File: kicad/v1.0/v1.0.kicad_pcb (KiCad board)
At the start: 2 copper layers, 71.4 x 69.6 mm, 50 parts, among them J1 USB_B_Micro, J2 9V_IN, J3 MOTOR, J4 LED, J5 BUTTON, Q1 IRF520, SW1 RESET, SW2 FLASH, U1 MCP2221AxSL, U2 MAX14872ETC+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

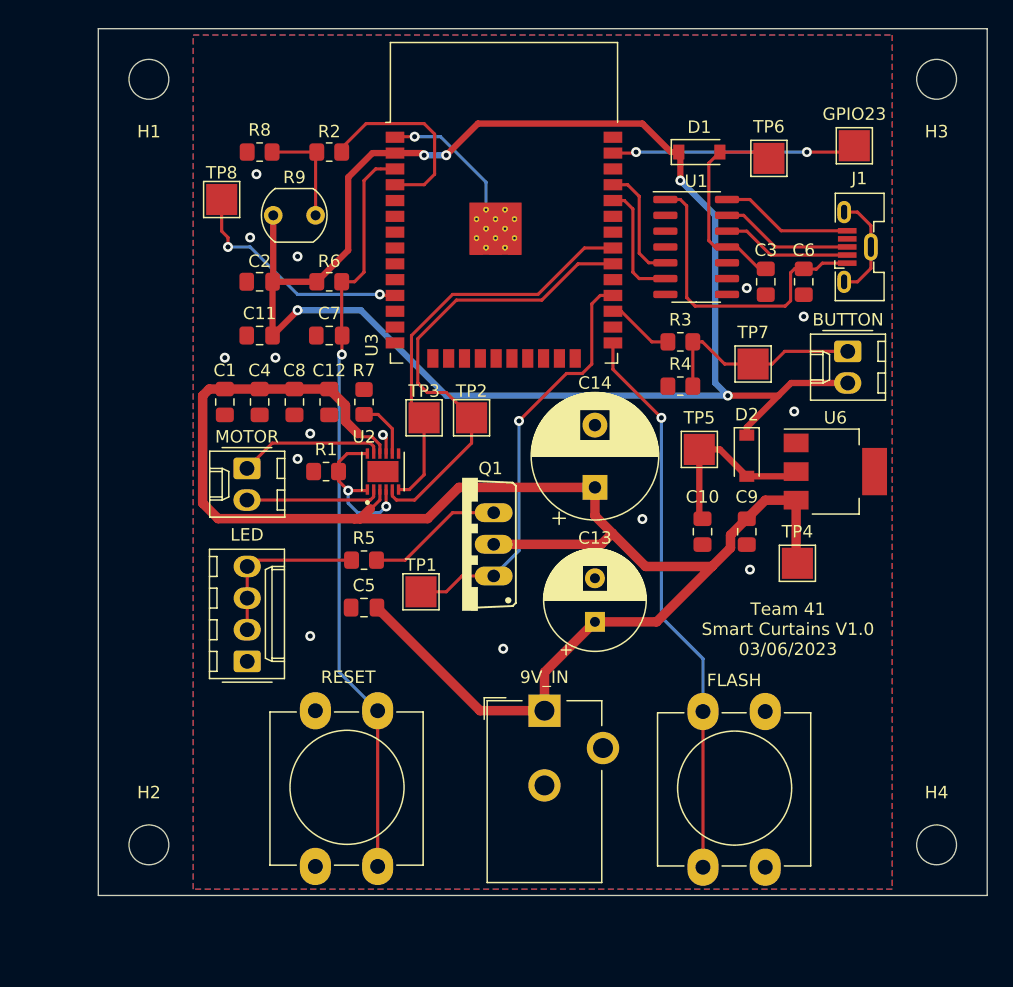
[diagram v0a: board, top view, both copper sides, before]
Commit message: v0.0 has been sent to TA for printing, all future changes must be on v1.0
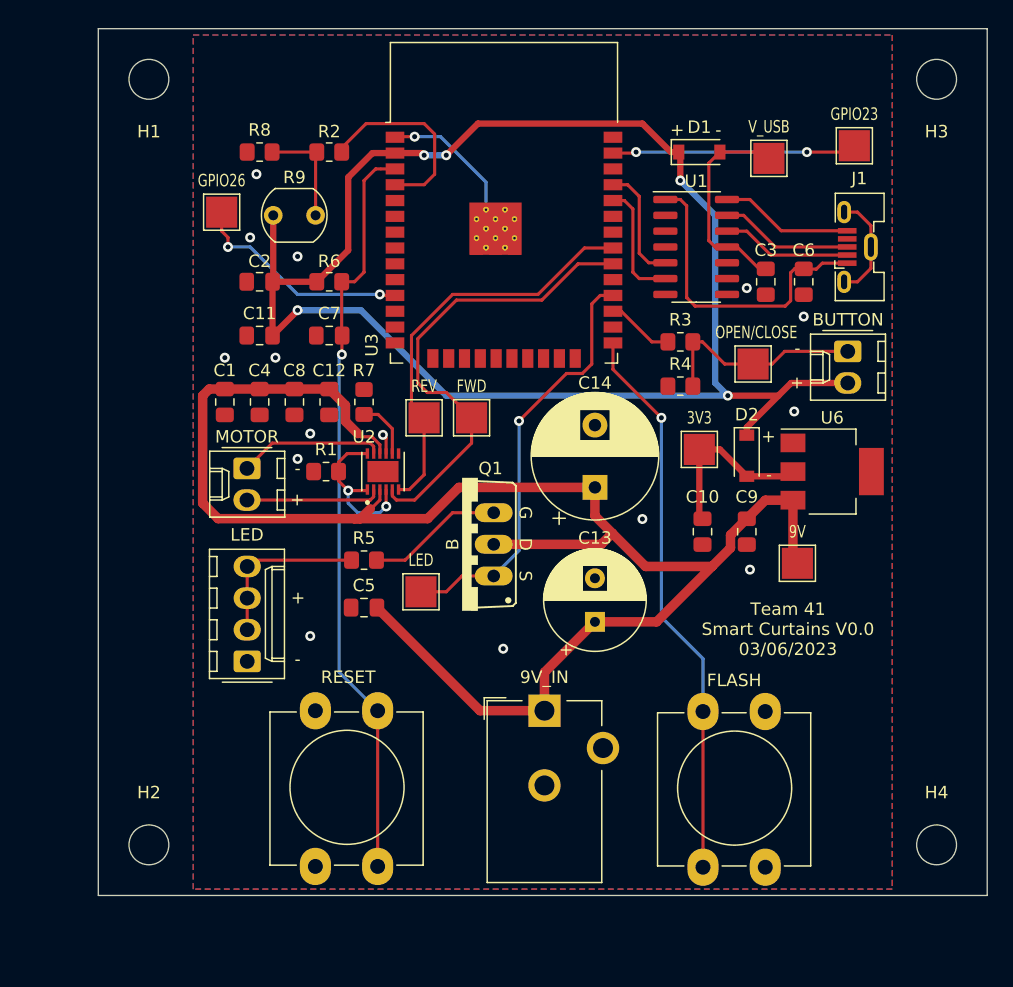
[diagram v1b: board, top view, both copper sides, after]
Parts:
- removed GPIO23: TestPoint, TestPoint:TestPoint_Pad_2.5x2.5mm
- added TP9: TestPoint, TestPoint:TestPoint_Pad_2.5x2.5mm, F.Cu at (173.5, 59.9)
- moved TP8 1.02 mm to (122.7, 65.3)
- moved U6 0.25 mm to (171.7, 86.1)
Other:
- board text added: "3V3"
- board text added: "9V"
- board text added: "FWD"
- board text added: "GPIO23"
- board text added: "GPIO26"
- board text added: "LED"
- board text added: "OPEN/CLOSE"
- board text added: "REV"
- board text added: "Team 41 Smart Curtains V0.0 03/06/2023"
- board text added: "V_USB"
- board text removed: "Team 41 Smart Curtains V1.0 03/06/2023"

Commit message: v0.0 pcb checkin
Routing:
- net Net-(J4-Pad2): track 13.7 -> 14.4 mm
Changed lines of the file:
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@@
       (effects (font (size 1 1) (thickness 0.15)))
     )
-    (fp_text user "S" (at -2.54 5.08 270 unlocked) (layer "F.SilkS")
-      (effects (font (size 1 1) (thickness 0.15)))
-    )
-    (fp_text user "G" (at 2.54 5.08 270 unlocked) (layer "F.SilkS")
+    (fp_text user "S" (at 2.54 5.08 270 unlocked) (layer "F.SilkS")
+      (effects (font (size 1 1) (thickness 0.15)))
+    )
+    (fp_text user "G" (at -2.794 5.08 270 unlocked) (layer "F.SilkS")
       (effects (font (size 1 1) (thickness 0.15)))
     )
@@
   (segment (start 133.604 89.408) (end 132.842 88.646) (width 0.254) (layer "B.Cu") (net 16))
   (segment (start 135.895714 88.905714) (end 135.884286 88.905714) (width 0.254) (layer "B.Cu") (net 16))
-  (segment (start 135.112 93.218) (end 137.414 93.218) (width 0.254) (layer "F.Cu") (net 17))
-  (segment (start 137.414 93.218) (end 141.224 89.408) (width 0.254) (layer "F.Cu") (net 17))
-  (segment (start 141.224 89.408) (end 144.526 89.408) (width 0.254) (layer "F.Cu") (net 17))
+  (segment (start 137.922 93.218) (end 135.112 93.218) (width 0.762) (layer "F.Cu") (net 17))
+  (segment (start 141.732 89.408) (end 137.922 93.218) (width 0.762) (layer "F.Cu") (net 17))
+  (segment (start 144.526 89.408) (end 141.732 89.408) (width 0.762) (layer "F.Cu") (net 17))
   (segment (start 126.73 60.452) (end 130.318 60.452) (width 0.25) (layer "F.Cu") (net 18))
   (segment (start 130.224 60.546) (end 130.318 60.452) (width 0.25) (layer "F.Cu") (net 18))
@@
   (segment (start 157.226 75.692) (end 158.512 75.692) (width 0.254) (layer "F.Cu") (net 56))
   (segment (start 124.734 93.706) (end 125.222 93.218) (width 0.254) (layer "F.Cu") (net 57))
-  (segment (start 124.734 98.806) (end 124.734 96.266) (width 0.254) (layer "F.Cu") (net 57))
   (segment (start 124.734 93.726) (end 124.734 93.706) (width 0.254) (layer "F.Cu") (net 57))
-  (segment (start 124.734 96.266) (end 124.734 93.726) (width 0.254) (layer "F.Cu") (net 57))
-  (segment (start 125.222 93.218) (end 133.112 93.218) (width 0.254) (layer "F.Cu") (net 57))
+  (segment (start 124.734 98.806) (end 124.734 96.266) (width 0.762) (layer "F.Cu") (net 57))
+  (segment (start 132.604 93.726) (end 124.734 93.726) (width 0.762) (layer "F.Cu") (net 57))
+  (segment (start 124.734 96.266) (end 124.734 93.726) (width 0.762) (layer "F.Cu") (net 57))
+  (segment (start 133.112 93.218) (end 132.604 93.726) (width 0.762) (layer "F.Cu") (net 57))
   (segment (start 163.068 77.47) (end 165.354 77.47) (width 0.254) (layer "F.Cu") (net 58))
   (segment (start 166.878 77.47) (end 167.894 76.454) (width 0.254) (layer "F.Cu") (net 58))

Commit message: getting ready to start designing PCB 1.0
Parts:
- removed R7: 10k, Resistor_SMD:R_0805_2012Metric_Pad1.20x1.40mm_HandSolder
- added C15: 22u, Capacitor_SMD:C_0805_2012Metric_Pad1.18x1.45mm_HandSolder, F.Cu at (134.6, 89.4)
- added R10: 1k, Resistor_SMD:R_0805_2012Metric_Pad1.20x1.40mm_HandSolder, F.Cu at (159.0, 102.1)
- U2: value MAX14872ETC+ -> ZXBM5210-SP; footprint MAX14872ETC_:SON50P300X300X80-13N -> Package_SO:Diodes_SO-8EP
- moved C5 11.5 mm to (145.0, 100.6)
- moved SW1 8.25 mm to (122.0, 117.8)
- moved U2 7.82 mm to (128.0, 87.9), turned to 180 degrees
- moved H1 6.37 mm to (110.5, 54.1)
- moved H2 6.37 mm to (110.5, 116.6)
- moved J3 5.87 mm to (118.9, 86.1)
- moved J4 5.85 mm to (118.9, 101.1)
- moved C1 5.84 mm to (117.1, 80.5)
- moved R1 5.61 mm to (130.6, 80.5), turned to -90 degrees
- moved C4 5.33 mm to (120.4, 80.5)
- moved C8 4.57 mm to (124.0, 80.5)
- moved C12 3.81 mm to (127.5, 80.5)
- moved J2 3.57 mm to (145.0, 105.6)
- moved SW2 2.07 mm to (163.4, 117.9)
- moved TP2 1.55 mm to (144.3, 81.5)
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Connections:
- J3 pad 1: Net-(J3-Pad1) -> Net-(U2-Pad7)
- J3 pad 2: Net-(J3-Pad2) -> Net-(U2-Pad1)
- R1 pad 1: /SNS -> +9V
- SW2 pad 1: Net-(SW2-Pad1) -> Net-(R10-Pad2)
- U2 pad 1: /SNS -> Net-(U2-Pad1)
- U2 pad 2: Net-(J3-Pad2) -> Net-(U2-Pad2)
- U2 pad 4: /SNS -> /FWD
- U2 pad 5: /FWD -> /REV
- U2 pad 6: /REV -> +9V
- U2 pad 7: unconnected-(U2-Pad7) -> Net-(U2-Pad7)
- U2 pad 8: Net-(R7-Pad1) -> GND
- U3 pad 25: Net-(SW2-Pad1) -> Net-(R10-Pad1)
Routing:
- net Net-(SW2-Pad1): track 45.1 -> 0.00 mm, vias 1 -> 0
- net Net-(R10-Pad1): track 0.00 -> 28.0 mm, vias 0 -> 2
- net Net-(R10-Pad2): track 0.00 -> 17.3 mm
- net +9V: track 137.7 -> 121.3 mm
- net Net-(U2-Pad1): track 0.00 -> 13.4 mm
- net /SNS: track 12.7 -> 0.00 mm, vias 2 -> 0
- net Net-(J3-Pad1): track 11.7 -> 0.00 mm
- net /REV: track 33.2 -> 44.9 mm, vias 0 -> 2
- net Net-(J3-Pad2): track 10.9 -> 0.00 mm
- net Net-(U2-Pad7): track 0.00 -> 7.67 mm
- net /FWD: track 38.1 -> 43.5 mm, vias 0 -> 2
- net Net-(J4-Pad2): track 14.4 -> 19.4 mm
- net Net-(R7-Pad1): track 4.75 -> 0.00 mm
- net Net-(U2-Pad2): track 0.00 -> 3.44 mm
- net Net-(C7-Pad1): track 60.7 -> 62.4 mm
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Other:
- board size 71.4 x 69.6 mm -> 77.2 x 69.6 mm

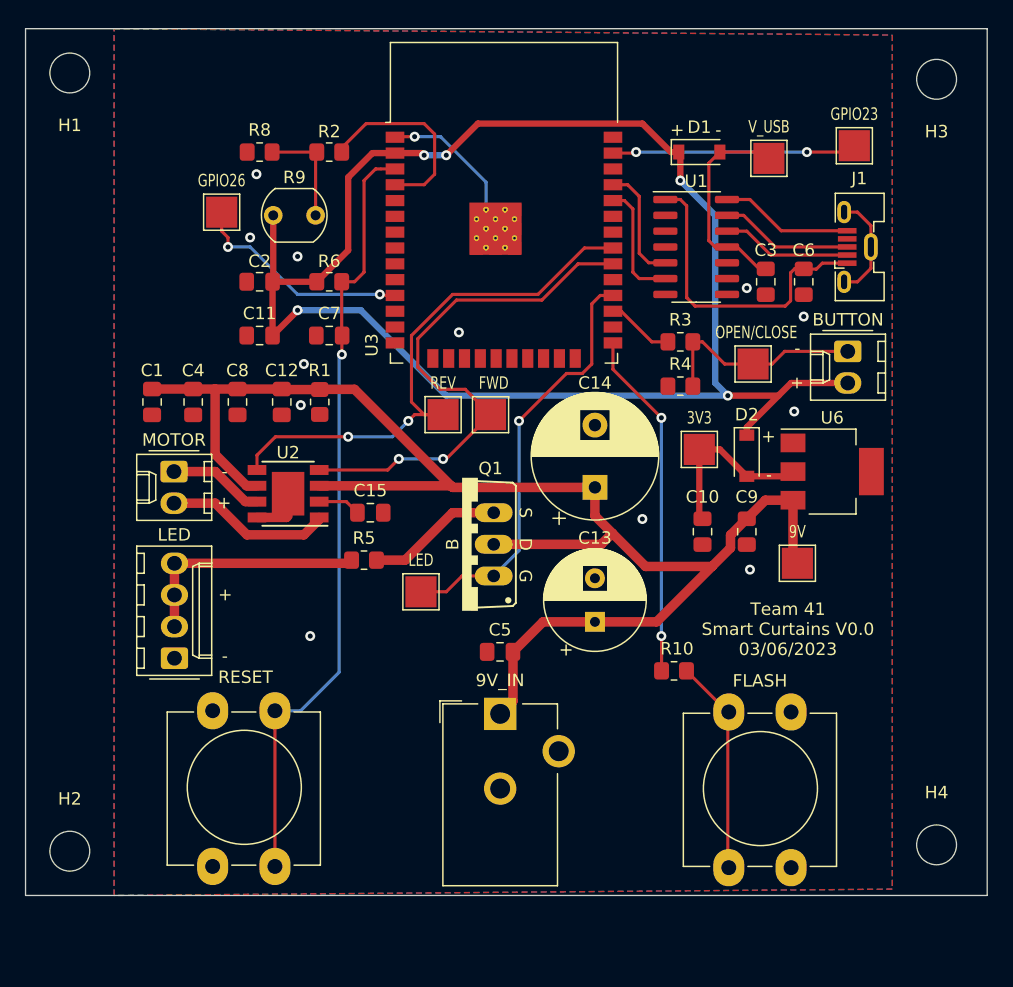
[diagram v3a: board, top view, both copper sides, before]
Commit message: PCB v1.0 is designed and sent to Nikhil, don't modify anything in here anymore
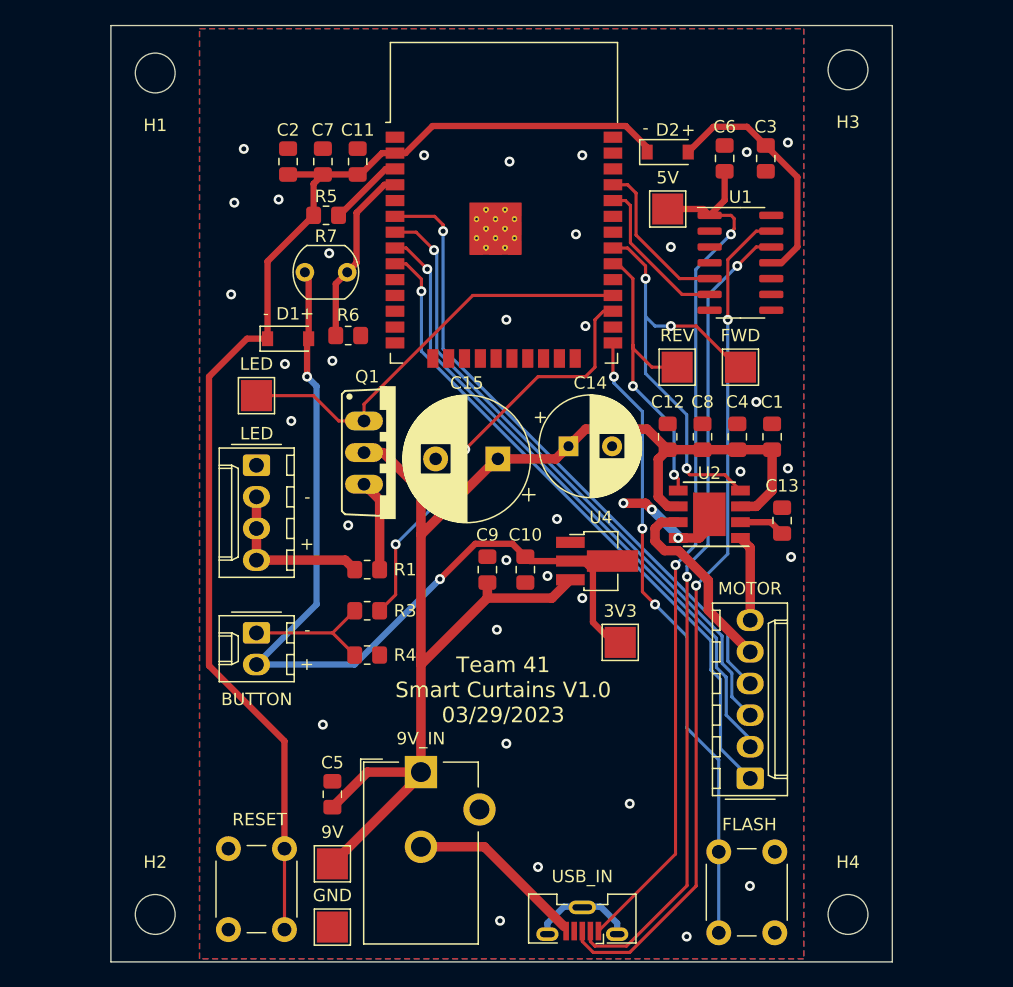
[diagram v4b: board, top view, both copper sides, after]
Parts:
- removed R10, R2: 1k, Resistor_SMD:R_0805_2012Metric_Pad1.20x1.40mm_HandSolder
- removed R8: 20k, Resistor_SMD:R_0805_2012Metric_Pad1.20x1.40mm_HandSolder
- removed R9: R_Photo, OptoDevice:R_LDR_5.1x4.3mm_P3.4mm_Vertical
- removed TP8, TP9: TestPoint, TestPoint:TestPoint_Pad_2.5x2.5mm
- removed U6: AZ1117-3.3, Package_TO_SOT_SMD:SOT-223
- added R7: R_Photo, OptoDevice:R_LDR_5.1x4.3mm_P3.4mm_Vertical, F.Cu at (129.4, 70.1)
- added U4: AZ1117-3.3, Package_TO_SOT_SMD:SOT-89-3_Handsoldering, F.Cu at (152.8, 93.3)
- C13: value 220u -> 22u; footprint Capacitor_THT:CP_Radial_D8.0mm_P3.50mm -> Capacitor_SMD:C_0805_2012Metric_Pad1.18x1.45mm_HandSolder
- C14: value 470u -> 220u; footprint Capacitor_THT:CP_Radial_D10.0mm_P5.00mm -> Capacitor_THT:CP_Radial_D8.0mm_P3.50mm
- C15: value 22u -> 470u; footprint Capacitor_SMD:C_0805_2012Metric_Pad1.18x1.45mm_HandSolder -> Capacitor_THT:CP_Radial_D10.0mm_P5.00mm
- J3: value MOTOR -> BUTTON; footprint Connector_Molex:Molex_KK-254_AE-6410-02A_1x02_P2.54mm_Vertical -> Connector_Molex:Molex_KK-254_AE-6410-06A_1x06_P2.54mm_Vertical
- R5: value 1k -> 10k
- R6: value 10k -> 20k
- SW1, SW2: footprint Button_Switch_THT:SW_PUSH-12mm_Wuerth-430476085716 -> Button_Switch_THT:SW_PUSH_6mm
- TP1: value TestPoint -> LED
- TP2: value TestPoint -> FWD
- TP3: value TestPoint -> REV
- TP4: value TestPoint -> 9V
- TP5: value TestPoint -> 3V3
- TP6: value TestPoint -> 5V
- TP7: value TestPoint -> GND
- moved J1 58.4 mm to (151.6, 122.2), turned to 180 degrees
- moved TP7 56.4 mm to (131.6, 122.7)
- moved J5 52.6 mm to (125.5, 99.1)
- moved J3 52.4 mm to (165.1, 110.7), turned to 90 degrees
- moved C1 49.9 mm to (166.9, 83.3), turned to 90 degrees
- moved TP4 44.5 mm to (131.6, 117.6)
- moved C4 43.8 mm to (164.1, 83.3), turned to 90 degrees
- moved C8 37.4 mm to (161.3, 83.3), turned to 90 degrees
- moved D1 36.3 mm to (128.0, 75.4)
- moved U2 33.9 mm to (161.8, 89.5)
- moved R3 33.1 mm to (134.4, 97.3), turned to 0 degrees
- moved R4 33.1 mm to (134.4, 100.8), turned to 0 degrees
- moved C12 31.1 mm to (158.5, 83.3), turned to 90 degrees
- moved R5 27.9 mm to (131.1, 65.5), turned to 0 degrees
- moved D2 25.2 mm to (158.5, 60.5), turned to 0 degrees
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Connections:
- C10 pad 1: Net-(C10-Pad1) -> /3V3_INPUT
- C11 pad 1: +3V3 -> Net-(C11-Pad1)
- C13 pad 1: +9V -> Net-(C13-Pad1)
- C15 pad 1: Net-(U2-Pad2) -> +9V
- C2 pad 1: +3V3 -> Net-(C11-Pad1)
- C3 pad 1: Net-(C3-Pad1) -> /3V3_USB
- C7 pad 1: Net-(C7-Pad1) -> Net-(C11-Pad1)
- D1 pad 1: +3V3 -> Net-(C11-Pad1)
- D1 pad 2: Net-(C3-Pad1) -> /3V3_INPUT
- D2 pad 1: +3V3 -> Net-(C11-Pad1)
- D2 pad 2: Net-(C10-Pad1) -> /3V3_USB
- J3 pad 1: Net-(U2-Pad7) -> /GPIO34
- J3 pad 2: Net-(U2-Pad1) -> /GPIO35
- J5 pad 2: +3V3 -> /3V3_INPUT
- R1 pad 1: +9V -> Net-(Q1-PadS)
- R1 pad 2: GND -> Net-(J4-Pad2)
- R5 pad 1: Net-(Q1-PadS) -> Net-(C11-Pad1)
- R5 pad 2: Net-(J4-Pad2) -> Net-(R5-Pad2)
- R6 pad 1: +3V3 -> Net-(R6-Pad1)
- R6 pad 2: Net-(C7-Pad1) -> GND
- SW1 pad 2: Net-(C7-Pad1) -> Net-(C11-Pad1)
- SW2 pad 1: Net-(R10-Pad2) -> Net-(SW2-Pad1)
- TP5 pad 1: Net-(C10-Pad1) -> /3V3_INPUT
- TP6 pad 1: Net-(C3-Pad1) -> Net-(C6-Pad1)
- TP7 pad 1: Net-(J5-Pad1) -> GND
- U1 pad 11: Net-(C3-Pad1) -> /3V3_USB
- U2 pad 1: Net-(U2-Pad1) -> Net-(J3-Pad6)
- U2 pad 2: Net-(U2-Pad2) -> Net-(C13-Pad1)
- U2 pad 7: Net-(U2-Pad7) -> Net-(J3-Pad5)
- U3 pad 11: Net-(TP8-Pad1) -> unconnected-(U3-Pad11)
- U3 pad 2: +3V3 -> Net-(C11-Pad1)
- U3 pad 25: Net-(R10-Pad1) -> Net-(SW2-Pad1)
- U3 pad 3: Net-(C7-Pad1) -> Net-(R5-Pad2)
- U3 pad 30: /FWD -> /REV
- U3 pad 31: /REV -> /FWD
- U3 pad 37: Net-(TP9-Pad1) -> unconnected-(U3-Pad37)
- U3 pad 4: /V_PHOTO -> Net-(R6-Pad1)
- U3 pad 6: unconnected-(U3-Pad6) -> /GPIO33
- U3 pad 7: unconnected-(U3-Pad7) -> /GPIO32
- U3 pad 8: unconnected-(U3-Pad8) -> /GPIO35
- U3 pad 9: unconnected-(U3-Pad9) -> /GPIO34
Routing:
- net +3V3: track 127.8 -> 0.00 mm, vias 5 -> 0
- net Net-(C11-Pad1): track 0.00 -> 99.4 mm
- net /3V3_INPUT: track 0.00 -> 74.4 mm, vias 0 -> 2
- net Net-(C7-Pad1): track 62.4 -> 0.00 mm, vias 1 -> 0
- net Net-(J1-Pad3): track 10.7 -> 68.3 mm, vias 0 -> 2
- net Net-(J1-Pad2): track 10.4 -> 65.6 mm, vias 0 -> 2
- net /GPIO34: track 0.00 -> 53.7 mm, vias 0 -> 1
- net /GPIO35: track 0.00 -> 52.4 mm, vias 0 -> 1
- net /GPIO32: track 0.00 -> 51.6 mm, vias 0 -> 1
- net /GPIO33: track 0.00 -> 51.2 mm, vias 0 -> 1
- net Net-(SW2-Pad1): track 0.00 -> 50.9 mm, vias 0 -> 3
- net Net-(C6-Pad1): track 25.2 -> 71.4 mm, vias 0 -> 2
- net Net-(R3-Pad2): track 5.43 -> 34.5 mm, vias 0 -> 2
- net Net-(R10-Pad1): track 28.0 -> 0.00 mm, vias 2 -> 0
- net /REV: track 44.9 -> 25.1 mm
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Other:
- board size 77.2 x 69.6 mm -> 62.7 x 75.2 mm
- board text added: "Team 41 Smart Curtains V1.0 03/29/2023"
- board text removed: "3V3"
- board text removed: "9V"
- board text removed: "FWD"
- board text removed: "GPIO23"
- board text removed: "GPIO26"
- board text removed: "LED"
- board text removed: "OPEN/CLOSE"
- board text removed: "REV"
- board text removed: "Team 41 Smart Curtains V0.0 03/06/2023"
- board text removed: "V_USB"
